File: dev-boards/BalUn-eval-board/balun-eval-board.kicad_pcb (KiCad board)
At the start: 4 copper layers, 44.5 x 55.8 mm, 11 parts, among them J1 SMA-142-0711-821, J2 SMA-142-0711-821, J3 SMA-142-0711-821, U1 NCS2-62+

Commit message: ignored a DRC rule
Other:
- board size 44.5 x 55.8 mm -> 44.1 x 55.8 mm
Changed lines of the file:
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@@
 		(sheetname "/")
 		(sheetfile "balun-eval-board.kicad_sch")
-		(units
-			(unit
-				(name "A")
-				(pins "1" "2" "3" "4" "5")
-			)
-		)
 		(attr smd)
 		(duplicate_pad_numbers_are_jumpers no)
@@
 		)
 		(fp_line
+			(start 5.08 -6.9215)
+			(end -5.08 -6.9215)
+			(stroke
+				(width 0.1524)
+				(type solid)
+			)
+			(layer "F.CrtYd")
+		)
+		(fp_line
+			(start -5.08 -6.9215)
+			(end -5.08 7.3025)
+			(stroke
+				(width 0.1524)
+				(type solid)
+			)
+			(layer "F.CrtYd")
+		)
+		(fp_line
+			(start 5.08 7.3025)
+			(end 5.08 -6.9215)
+			(stroke
+				(width 0.1524)
+				(type solid)
+			)
+			(layer "F.CrtYd")
+		)
+		(fp_line
+			(start -5.08 7.3025)
+			(end 5.08 7.3025)
+			(stroke
+				(width 0.1524)
+				(type solid)
+			)
+			(layer "F.CrtYd")
+		)
+		(fp_line
+			(start 3.175 -6.6675)
+			(end -3.175 -6.6675)
+			(stroke
+				(width 0.0254)
+				(type solid)
+			)
+			(layer "F.Fab")
+		)
+		(fp_line
+			(start -3.175 -6.6675)
+			(end -3.175 6.6675)
+			(stroke
+				(width 0.0254)
+				(type solid)
+			)
+			(layer "F.Fab")
+		)
+		(fp_line
 			(start 3.175 2.8575)
 			(end -3.175 2.8575)
-			(stroke
-				(width 0.0254)
-				(type solid)
-			)
-			(layer "Edge.Cuts")
-		)
-		(fp_line
-			(start 5.08 -6.9215)
-			(end -5.08 -6.9215)
-			(stroke
-				(width 0.1524)
-				(type solid)
-			)
-			(layer "F.CrtYd")
-		)
-		(fp_line
-			(start -5.08 -6.9215)
-			(end -5.08 7.3025)
-			(stroke
-				(width 0.1524)
-				(type solid)
-			)
-			(layer "F.CrtYd")
-		)
-		(fp_line
-			(start 5.08 7.3025)
-			(end 5.08 -6.9215)
-			(stroke
-				(width 0.1524)
-				(type solid)
-			)
-			(layer "F.CrtYd")
-		)
-		(fp_line
-			(start -5.08 7.3025)
-			(end 5.08 7.3025)
-			(stroke
-				(width 0.1524)
-				(type solid)
-			)
-			(layer "F.CrtYd")
-		)
-		(fp_line
-			(start 3.175 -6.6675)
-			(end -3.175 -6.6675)
-			(stroke
-				(width 0.0254)
-				(type solid)
-			)
-			(layer "F.Fab")
-		)
-		(fp_line
-			(start -3.175 -6.6675)
-			(end -3.175 6.6675)
 			(stroke
 				(width 0.0254)
@@
 		(sheetname "/")
 		(sheetfile "balun-eval-board.kicad_sch")
-		(units
-			(unit
-				(name "A")
-				(pins "1" "2" "3" "4" "5")
-			)
-		)
 		(attr smd)
 		(duplicate_pad_numbers_are_jumpers no)
@@
 		)
 		(fp_line
+			(start -5.08 7.3025)
+			(end 5.08 7.3025)
+			(stroke
+				(width 0.1524)
+				(type solid)
+			)
+			(layer "F.CrtYd")
+		)
+		(fp_line
+			(start 5.08 7.3025)
+			(end 5.08 -6.9215)
+			(stroke
+				(width 0.1524)
+				(type solid)
+			)
+			(layer "F.CrtYd")
+		)
+		(fp_line
+			(start -5.08 -6.9215)
+			(end -5.08 7.3025)
+			(stroke
+				(width 0.1524)
+				(type solid)
+			)
+			(layer "F.CrtYd")
+		)
+		(fp_line
+			(start 5.08 -6.9215)
+			(end -5.08 -6.9215)
+			(stroke
+				(width 0.1524)
+				(type solid)
+			)
+			(layer "F.CrtYd")
+		)
+		(fp_line
+			(start -3.175 6.6675)
+			(end 3.175 6.6675)
+			(stroke
+				(width 0.0254)
+				(type solid)
+			)
+			(layer "F.Fab")
+		)
+		(fp_line
+			(start 3.175 6.6675)
+			(end 3.175 -6.6675)
+			(stroke
+				(width 0.0254)
+				(type solid)
+			)
+			(layer "F.Fab")
+		)
+		(fp_line
 			(start 3.175 2.8575)
 			(end -3.175 2.8575)
-			(stroke
-				(width 0.0254)
-				(type solid)
-			)
-			(layer "Edge.Cuts")
-		)
-		(fp_line
-			(start -5.08 7.3025)
-			(end 5.08 7.3025)
-			(stroke
-				(width 0.1524)
-				(type solid)
-			)
-			(layer "F.CrtYd")
-		)
-		(fp_line
-			(start 5.08 7.3025)
-			(end 5.08 -6.9215)
-			(stroke
-				(width 0.1524)
-				(type solid)
-			)
-			(layer "F.CrtYd")
-		)
-		(fp_line
-			(start -5.08 -6.9215)
-			(end -5.08 7.3025)
-			(stroke
-				(width 0.1524)
-				(type solid)
-			)
-			(layer "F.CrtYd")
-		)
-		(fp_line
-			(start 5.08 -6.9215)
-			(end -5.08 -6.9215)
-			(stroke
-				(width 0.1524)
-				(type solid)
-			)
-			(layer "F.CrtYd")
-		)
-		(fp_line
-			(start -3.175 6.6675)
-			(end 3.175 6.6675)
-			(stroke
-				(width 0.0254)
-				(type solid)
-			)
-			(layer "F.Fab")
-		)
-		(fp_line
-			(start 3.175 6.6675)
-			(end 3.175 -6.6675)
 			(stroke
 				(width 0.0254)
@@
 		(sheetname "/")
 		(sheetfile "balun-eval-board.kicad_sch")
-		(units
-			(unit
-				(name "A")
-				(pins "1" "2" "3" "4" "5")
-			)
-		)
 		(attr smd)
 		(duplicate_pad_numbers_are_jumpers no)
@@
 		)
 		(fp_line
+			(start 5.08 -6.9215)
+			(end -5.08 -6.9215)
+			(stroke
+				(width 0.1524)
+				(type solid)
+			)
+			(layer "F.CrtYd")
+		)
+		(fp_line
+			(start -5.08 -6.9215)
+			(end -5.08 7.3025)
+			(stroke
+				(width 0.1524)
+				(type solid)
+			)
+			(layer "F.CrtYd")
+		)
+		(fp_line
+			(start 5.08 7.3025)
+			(end 5.08 -6.9215)
+			(stroke
+				(width 0.1524)
+				(type solid)
+			)
+			(layer "F.CrtYd")
+		)
+		(fp_line
+			(start -5.08 7.3025)
+			(end 5.08 7.3025)
+			(stroke
+				(width 0.1524)
+				(type solid)
+			)
+			(layer "F.CrtYd")
+		)
+		(fp_line
+			(start 3.175 -6.6675)
+			(end -3.175 -6.6675)
+			(stroke
+				(width 0.0254)
+				(type solid)
+			)
+			(layer "F.Fab")
+		)
+		(fp_line
+			(start -3.175 -6.6675)
+			(end -3.175 6.6675)
+			(stroke
+				(width 0.0254)
+				(type solid)
+			)
+			(layer "F.Fab")
+		)
+		(fp_line
 			(start 3.175 2.8575)
 			(end -3.175 2.8575)
-			(stroke
-				(width 0.0254)
-				(type solid)
-			)
-			(layer "Edge.Cuts")
-		)
-		(fp_line
-			(start 5.08 -6.9215)
-			(end -5.08 -6.9215)
-			(stroke
-				(width 0.1524)
-				(type solid)
-			)
-			(layer "F.CrtYd")
-		)
-		(fp_line
-			(start -5.08 -6.9215)
-			(end -5.08 7.3025)
-			(stroke
-				(width 0.1524)
-				(type solid)
-			)
-			(layer "F.CrtYd")
-		)
-		(fp_line
-			(start 5.08 7.3025)
-			(end 5.08 -6.9215)
-			(stroke
-				(width 0.1524)
-				(type solid)
-			)
-			(layer "F.CrtYd")
-		)
-		(fp_line
-			(start -5.08 7.3025)
-			(end 5.08 7.3025)
-			(stroke
-				(width 0.1524)
-				(type solid)
-			)
-			(layer "F.CrtYd")
-		)
-		(fp_line
-			(start 3.175 -6.6675)
-			(end -3.175 -6.6675)
-			(stroke
-				(width 0.0254)
-				(type solid)
-			)
-			(layer "F.Fab")
-		)
-		(fp_line
-			(start -3.175 -6.6675)
-			(end -3.175 6.6675)
 			(stroke
 				(width 0.0254)
@@
 	)
 	(gr_line
-		(start 103.85 74)
-		(end 103.85 129.82)
+		(start 104.0475 74)
+		(end 104.0475 129.82)
 		(stroke
 			(width 0.05)
@@
 	)
 	(gr_line
-		(start 103.85 74)
-		(end 148.3 74)
+		(start 104.0475 74)
+		(end 148.1305 74)
 		(stroke
 			(width 0.05)
@@
 	)
 	(gr_line
-		(start 103.85 129.82)
-		(end 148.3 129.82)
+		(start 104.0475 129.82)
+		(end 148.1305 129.82)
 		(stroke
 			(width 0.05)
@@
 	)
 	(gr_line
-		(start 148.3 74)
-		(end 148.3 129.82)
+		(start 148.1305 74)
+		(end 148.1305 129.82)
 		(stroke
 			(width 0.05)

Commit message: made changes to BalUn board
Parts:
- removed R1, R2, R3, R4: 0, oresat-passives:0603-B-NOSILK
- J1, J2, J3: value SMA-142-0711-821 -> SMA-142-0711-201; footprint oresat-connectors:SMA-142-0711-821 -> oresat-connectors:SMA-J-P-H-ST-EM1
- moved J1 4.77 mm to (106.0, 94.8)
- moved J2 4.77 mm to (106.0, 109.0)
- moved J3 4.74 mm to (146.2, 102.6)
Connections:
- TP1 pad 1: Net-(R2-Pad1) -> Net-(J1-Pad1)
- TP2 pad 1: Net-(R1-Pad2) -> Net-(J2-Pad1)
- U1 pad 1: Net-(R2-Pad2) -> Net-(J1-Pad1)
- U1 pad 3: Net-(R1-Pad1) -> Net-(J2-Pad1)
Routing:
- net Net-(J2-Pad1): track 10.8 -> 38.4 mm
- net Net-(J1-Pad1): track 10.8 -> 38.4 mm
- net Net-(R1-Pad2): track 12.3 -> 0.00 mm
- net Net-(R2-Pad1): track 12.2 -> 0.00 mm
- net Net-(R2-Pad2): track 12.1 -> 0.00 mm
- net Net-(R1-Pad1): track 12.1 -> 0.00 mm
- net GND: vias 130 -> 122

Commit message: made changes to NCS2-62+ balUn dev board
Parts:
- added ?: , , B.Cu at (121.6, 125.8)
- added ?: , , B.Cu at (121.6, 78.0)
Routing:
- net Net-(J2-Pad1): vias 0 -> 9
- net Net-(J1-Pad1): vias 0 -> 9
- net GND: vias 122 -> 222
- added copper zone on In1.Cu, net GND
- added copper zone on In2.Cu, net GND
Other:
- board text added: "NCS-62+ BalUn Dev Board Version 1.0 10/11/2026 JJDLSR"

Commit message: last changes to NCS2-62+ BalUn dev board
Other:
- board text added: "<-- No copper pour around pads because they will be used for for antenna elements"
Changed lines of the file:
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@@
 		(capping no)
 		(filling no)
-		(zone_defaults)
 		(pcbplotparams
 			(layerselection 0x00000000_00000000_55555555_5755f5ff)
@@
 		(layer "Edge.Cuts")
 	)
+	(gr_text "<-- No copper pour around pads\n	 because they will be used for \n	 for antenna elements"
+		(at 127.3 80.78 0)
+		(layer "F.SilkS")
+		(effects
+			(font
+				(size 0.7 0.7)
+				(thickness 0.125)
+				(bold yes)
+			)
+			(justify left bottom)
+		)
+	)
 	(gr_text "NCS-62+ BalUn Dev Board\nVersion 1.0\n10/11/2026\nJJDLSR\n"

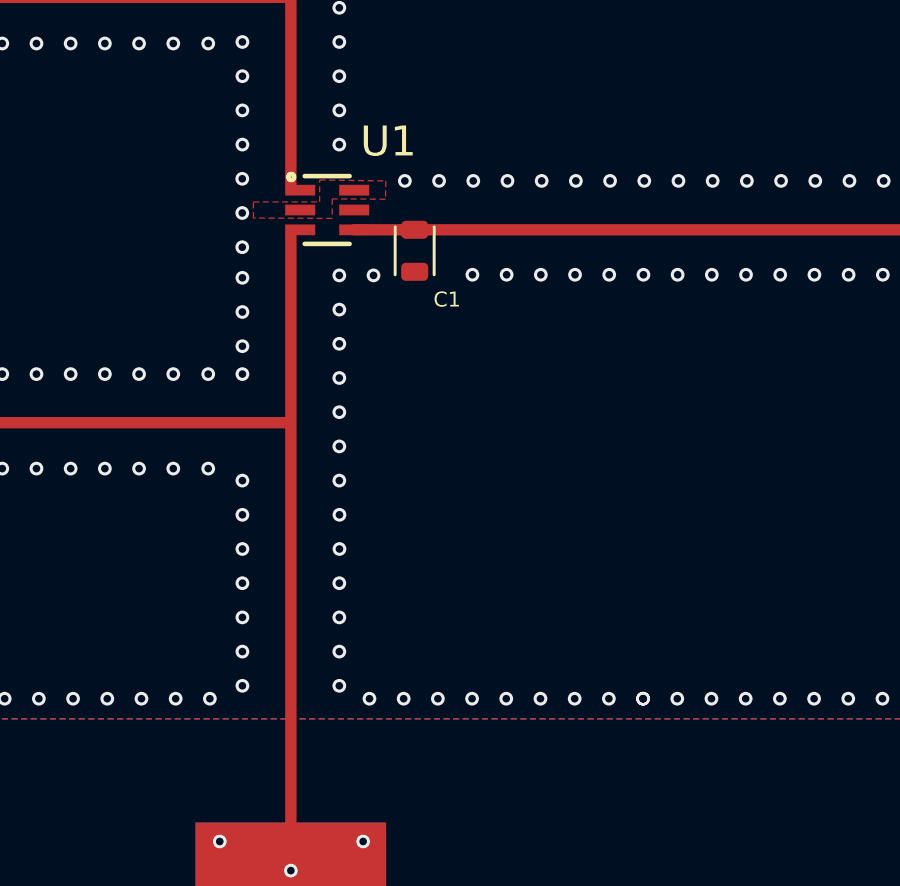
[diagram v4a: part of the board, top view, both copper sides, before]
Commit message: final layout for NCS2-62+ BalUn dev board
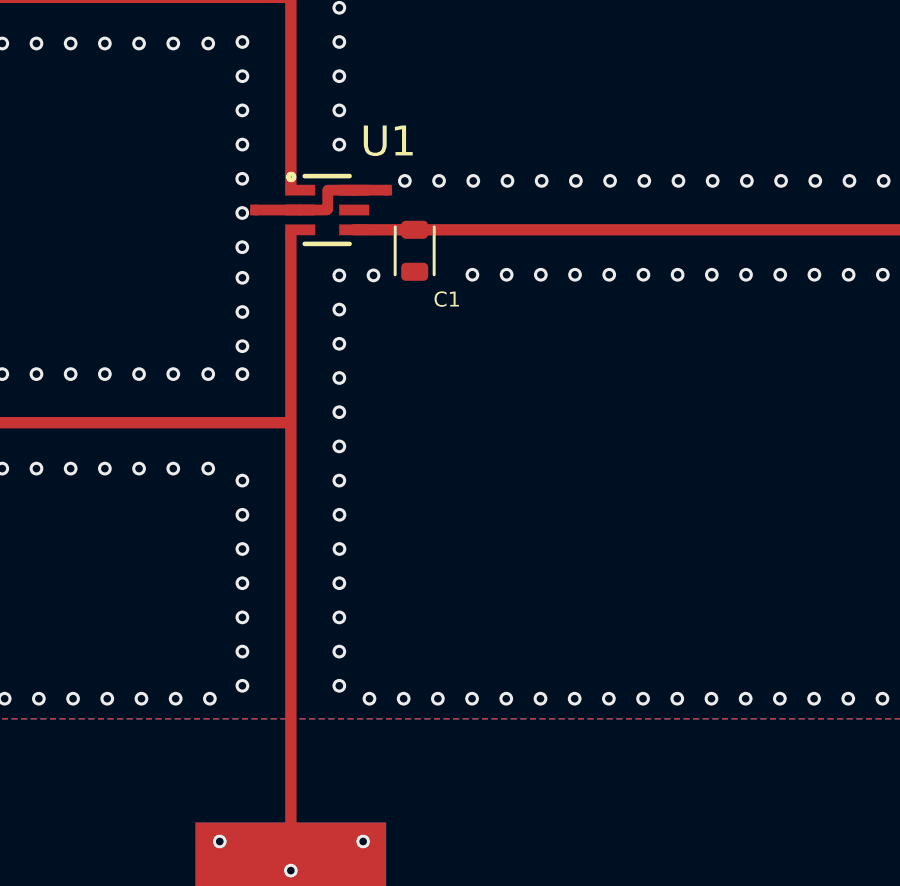
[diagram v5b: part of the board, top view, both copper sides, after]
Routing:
- net GND: track 0.00 -> 5.01 mm, vias 222 -> 221
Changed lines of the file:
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@@
+	(gr_poly
+		(pts
+			(xy 120.214285 101.73) (xy 120.214285 102.09) (xy 120.470286 102.09) (xy 120.46 101.73)
+		)
+		(stroke
+			(width 0.001)
+			(type solid)
+		)
+		(fill yes)
+		(layer "F.Cu")
+		(net "GND")
+	)
+	(gr_poly
+		(pts
+			(xy 124.69 101.07) (xy 124.69 101.429646) (xy 124.945715 101.429646) (xy 124.935439 101.07)
+		)
+		(stroke
+			(width 0.001)
+			(type solid)
+		)
+		(fill yes)
+		(layer "F.Cu")
+		(net "GND")
+	)
 	(gr_poly
 		(pts
@@
 		(net "Net-(J2-Pad1)")
 	)
+	(segment
+		(start 122.8 101.26)
+		(end 122.81 101.25)
+		(width 0.127)
+		(layer "F.Cu")
+		(net "GND")
+	)
+	(segment
+		(start 122.77 101.91)
+		(end 122.8 101.88)
+		(width 0.127)
+		(layer "F.Cu")
+		(net "GND")
+	)
+	(segment
+		(start 123.68 101.25)
+		(end 124.76 101.25)
+		(width 0.36)
+		(layer "F.Cu")
+		(net "GND")
+	)
+	(segment
+		(start 122.8 101.88)
+		(end 122.8 101.26)
+		(width 0.36)
+		(layer "F.Cu")
+		(net "GND")
+	)
+	(segment
+		(start 121.88 101.91)
+		(end 120.39 101.91)
+		(width 0.36)
+		(layer "F.Cu")
+		(net "GND")
+	)
+	(segment
+		(start 121.88 101.91)
+		(end 122.77 101.91)
+		(width 0.36)
+		(layer "F.Cu")
+		(net "GND")
+	)
+	(segment
+		(start 122.81 101.25)
+		(end 123.68 101.25)
+		(width 0.36)
+		(layer "F.Cu")
+		(net "GND")
+	)
 	(via
 		(at 119.95 100.87)
@@
 	(via
 		(at 144.92 85.62)
-		(size 0.4572)
-		(drill 0.254)
-		(layers "F.Cu" "B.Cu")
-		(free yes)
-		(net "GND")
-	)
-	(via
-		(at 133.31 118.2)
 		(size 0.4572)
 		(drill 0.254)
@@
 	)
 	(zone
-		(net "GND")
-		(layer "F.Cu")
-		(hatch edge 0.5)
-		(priority 2)
-		(connect_pads yes
-			(clearance 0.127)
-		)
-		(min_thickness 0.25)
-		(fill yes
-			(thermal_gap 0.5)
-			(thermal_bridge_width 1)
-			(island_removal_mode 0)
-		)
-		(polygon
-			(pts
-				(xy 120.32122 101.64) (xy 122.53 101.64) (xy 122.53 100.91) (xy 124.735071 100.940626) (xy 124.725077 101.550261)
-				(xy 122.95 101.54) (xy 122.95 102.19) (xy 120.318789 102.178118)
-			)
-		)
-	)
-	(zone
